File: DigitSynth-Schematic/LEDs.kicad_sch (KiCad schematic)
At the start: 7 parts, among them J6 Adafruit TLC59711

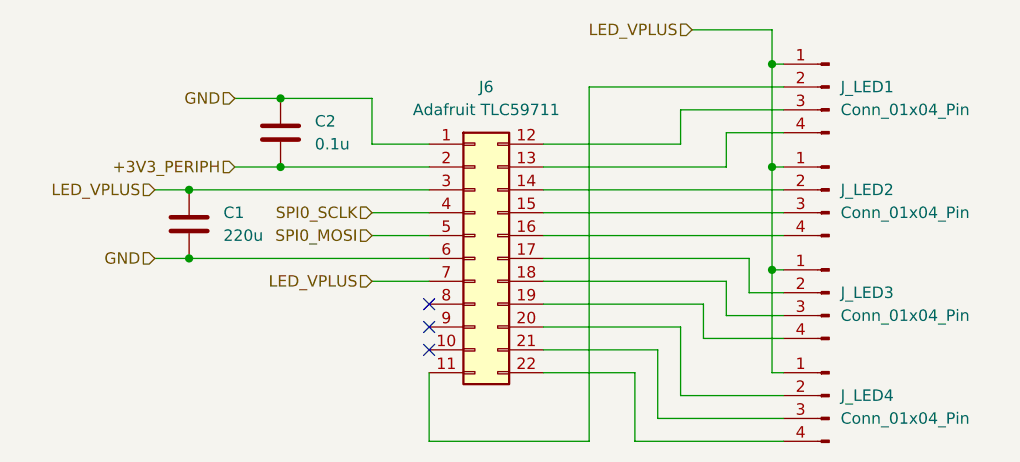
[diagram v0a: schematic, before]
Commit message: removed power schematic sheet as RPI5 has decoupling capacitors; fixed component value errors; buttons removed from RPI5 sheet and added to ADC analog inputs; LED_VPLUS power line removed and replaced by +5V_PERIPH
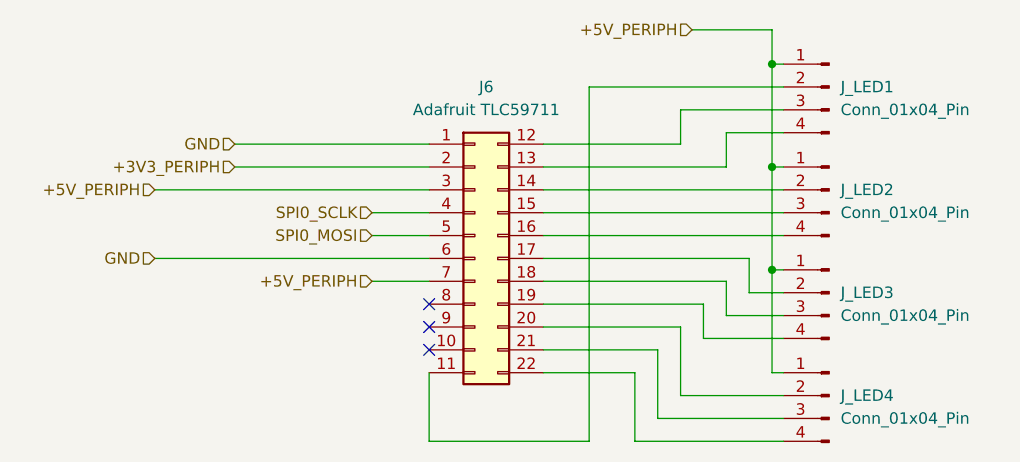
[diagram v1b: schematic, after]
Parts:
- removed C1: 220u, symbol Device:C
- removed C2: 0.1u, symbol Device:C
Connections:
- net LED_VPLUS renamed +5V_PERIPH
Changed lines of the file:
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@@
 	(paper "A4")
-	(junction
-		(at 137.16 69.85)
-		(diameter 0)
-		(color 0 0 0 0)
-	)
-	(junction
-		(at 147.32 52.07)
-		(diameter 0)
-		(color 0 0 0 0)
-	)
 	(junction
 		(at 201.93 48.26)
@@
 		(color 0 0 0 0)
 	)
-	(junction
-		(at 137.16 62.23)
-		(diameter 0)
-		(color 0 0 0 0)
-	)
-	(junction
-		(at 147.32 59.69)
-		(diameter 0)
-		(color 0 0 0 0)
-	)
 	(no_connect
 		(at 163.83 74.93)
@@
 	(wire
 		(pts
-			(xy 133.35 69.85) (xy 137.16 69.85)
+			(xy 133.35 69.85) (xy 163.83 69.85)
 		)
 		(stroke
@@
 	(wire
 		(pts
-			(xy 147.32 52.07) (xy 157.48 52.07)
+			(xy 142.24 57.15) (xy 163.83 57.15)
 		)
 		(stroke
@@
 	(wire
 		(pts
+			(xy 133.35 62.23) (xy 163.83 62.23)
+		)
+		(stroke
+			(width 0)
+			(type default)
+		)
+	)
+	(wire
+		(pts
 			(xy 201.93 44.45) (xy 201.93 48.26)
 		)
@@
 	(wire
 		(pts
-			(xy 133.35 62.23) (xy 137.16 62.23)
-		)
-		(stroke
-			(width 0)
-			(type default)
-		)
-	)
-	(wire
-		(pts
 			(xy 176.53 59.69) (xy 196.85 59.69)
 		)
@@
 	(wire
 		(pts
-			(xy 142.24 59.69) (xy 147.32 59.69)
-		)
-		(stroke
-			(width 0)
-			(type default)
-		)
-	)
-	(wire
-		(pts
-			(xy 137.16 62.23) (xy 163.83 62.23)
+			(xy 142.24 59.69) (xy 163.83 59.69)
 		)
 		(stroke
@@
 	(wire
 		(pts
-			(xy 157.48 57.15) (xy 163.83 57.15)
-		)
-		(stroke
-			(width 0)
-			(type default)
-		)
-	)
-	(wire
-		(pts
 			(xy 157.48 67.31) (xy 163.83 67.31)
 		)
@@
 	(wire
 		(pts
-			(xy 137.16 69.85) (xy 163.83 69.85)
-		)
-		(stroke
-			(width 0)
-			(type default)
-		)
-	)
-	(wire
-		(pts
-			(xy 142.24 52.07) (xy 147.32 52.07)
-		)
-		(stroke
-			(width 0)
-			(type default)
-		)
-	)
-	(wire
-		(pts
 			(xy 181.61 50.8) (xy 203.2 50.8)
 		)
@@
 		(pts
 			(xy 189.23 87.63) (xy 203.2 87.63)
-		)
-		(stroke
-			(width 0)
-			(type default)
-		)
-	)
-	(wire
-		(pts
-			(xy 157.48 52.07) (xy 157.48 57.15)
-		)
-		(stroke
-			(width 0)
-			(type default)
-		)
-	)
-	(wire
-		(pts
-			(xy 147.32 59.69) (xy 163.83 59.69)
 		)
 		(stroke
@@
 	(hierarchical_label "GND"
 		(shape input)
-		(at 142.24 52.07 180)
+		(at 142.24 57.15 180)
 		(effects
 			(font
@@
 		)
 	)
-	(hierarchical_label "LED_VPLUS"
+	(hierarchical_label "+5V_PERIPH"
 		(shape input)
 		(at 157.48 72.39 180)
@@
 		)
 	)
-	(hierarchical_label "LED_VPLUS"
+	(hierarchical_label "+5V_PERIPH"
 		(shape input)
 		(at 193.04 44.45 180)
@@
 		)
 	)
-	(hierarchical_label "LED_VPLUS"
+	(hierarchical_label "+5V_PERIPH"
 		(shape input)
 		(at 133.35 62.23 180)
@@
 	)
 	(symbol
-		(lib_id "Device:C")
-		(at 147.32 55.88 0)
-		(unit 1)
-		(exclude_from_sim no)
-		(in_bom yes)
-		(on_board yes)
-		(dnp no)
-		(fields_autoplaced yes)
-		(property "Reference" "C2"
-			(at 151.13 54.6099 0)
-			(effects
-				(font
-					(size 1.27 1.27)
-				)
-				(justify left)
-			)
-		)
-		(property "Value" "0.1u"
-			(at 151.13 57.1499 0)
-			(effects
-				(font
-					(size 1.27 1.27)
-				)
-				(justify left)
-			)
-		)
-		(property "Footprint" ""
-			(at 148.2852 59.69 0)
-			(effects
-				(font
-					(size 1.27 1.27)
-				)
-				(hide yes)
-			)
-		)
-		(property "Datasheet" "~"
-			(at 147.32 55.88 0)
-			(effects
-				(font
-					(size 1.27 1.27)
-				)
-				(hide yes)
-			)
-		)
-		(property "Description" "Unpolarized capacitor"
-			(at 147.32 55.88 0)
-			(effects
-				(font
-					(size 1.27 1.27)
-				)
-				(hide yes)
-			)
-		)
-		(pin "2"
-		)
-		(pin "1"
-		)
-		(instances
-			(project ""
-				(path "/ad908932-4812-48b1-9c87-6bb086cd45d9/62a7dce8-d0c0-4114-8523-fa7c8317d31c"
-					(reference "C2")
-					(unit 1)
-				)
-			)
-		)
-	)
-	(symbol
 		(lib_id "Connector_Generic:Conn_02x11_Top_Bottom")
 		(at 168.91 69.85 0)
@@
 					(unit 1)
 				)
-			)
-		)
-	)
-	(symbol
-		(lib_id "Device:C")
-		(at 137.16 66.04 0)
-		(unit 1)
-		(exclude_from_sim no)
-		(in_bom yes)
-		(on_board yes)
-		(dnp no)
-		(property "Reference" "C1"
-			(at 140.97 64.7699 0)
-			(effects
-				(font
-					(size 1.27 1.27)
-				)
-				(justify left)
-			)
-		)
-		(property "Value" "220u"
-			(at 140.97 67.3099 0)
-			(effects
-				(font
-					(size 1.27 1.27)
-				)
-				(justify left)
-			)
-		)
-		(property "Footprint" ""
-			(at 138.1252 69.85 0)
-			(effects
-				(font
-					(size 1.27 1.27)
-				)
-				(hide yes)
-			)
-		)
-		(property "Datasheet" "~"
-			(at 137.16 66.04 0)
-			(effects
-				(font
-					(size 1.27 1.27)
-				)
-				(hide yes)
-			)
-		)
-		(property "Description" "Unpolarized capacitor"
-			(at 137.16 66.04 0)
-			(effects
-				(font
-					(size 1.27 1.27)
-				)
-				(hide yes)
-			)
-		)
-		(pin "2"
-		)
-		(pin "1"
-		)
-		(instances
-			(project "DigitSynth"
-				(path "/ad908932-4812-48b1-9c87-6bb086cd45d9/62a7dce8-d0c0-4114-8523-fa7c8317d31c"
-					(reference "C1")
-					(unit 1)
-				)

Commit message: updated schematic for PCB design
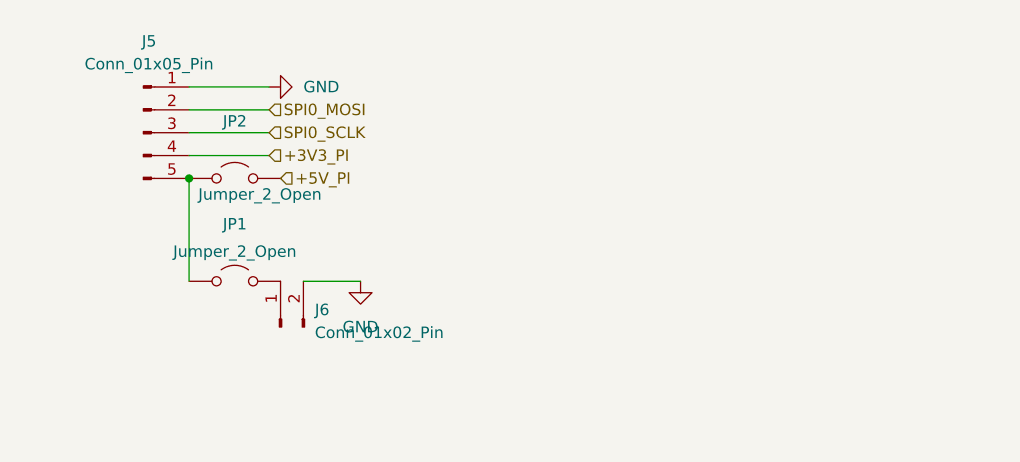
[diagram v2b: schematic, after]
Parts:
- removed J6: Adafruit TLC59711, symbol Connector_Generic:Conn_02x11_Top_Bottom
- removed J_LED1, J_LED2, J_LED3, J_LED4: Conn_01x04_Pin, symbol Connector:Conn_01x04_Pin
- added J5: Conn_01x05_Pin, symbol Connector:Conn_01x05_Pin
- added J6: Conn_01x02_Pin, symbol Connector:Conn_01x02_Pin
- added JP1, JP2: Jumper_2_Open, symbol Jumper:Jumper_2_Open
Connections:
- net GND: now also J5.1 (Pin_1), J6.2 (Pin_2)
- net SPI0_MOSI: now also J5.2 (Pin_2)
- net SPI0_SCLK: now also J5.3 (Pin_3)
- new net: J5.5 (Pin_5), JP1.1 (A), JP2.1 (A)
- new net: J6.1 (Pin_1), JP1.2 (B)
- new net +3V3_PI: J5.4 (Pin_4)
- new net +5V_PI: JP2.2 (B)
- no-connect marks 3 -> 0
